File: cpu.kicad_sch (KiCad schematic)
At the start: 50 parts, among them IC12 DS2401+, IC13 ARM250, IC20 74HC138, IC27 74AC32, IC8 74HCT14, X100 40.0MHz, X4 72.0MHz, X5 25.175MHz

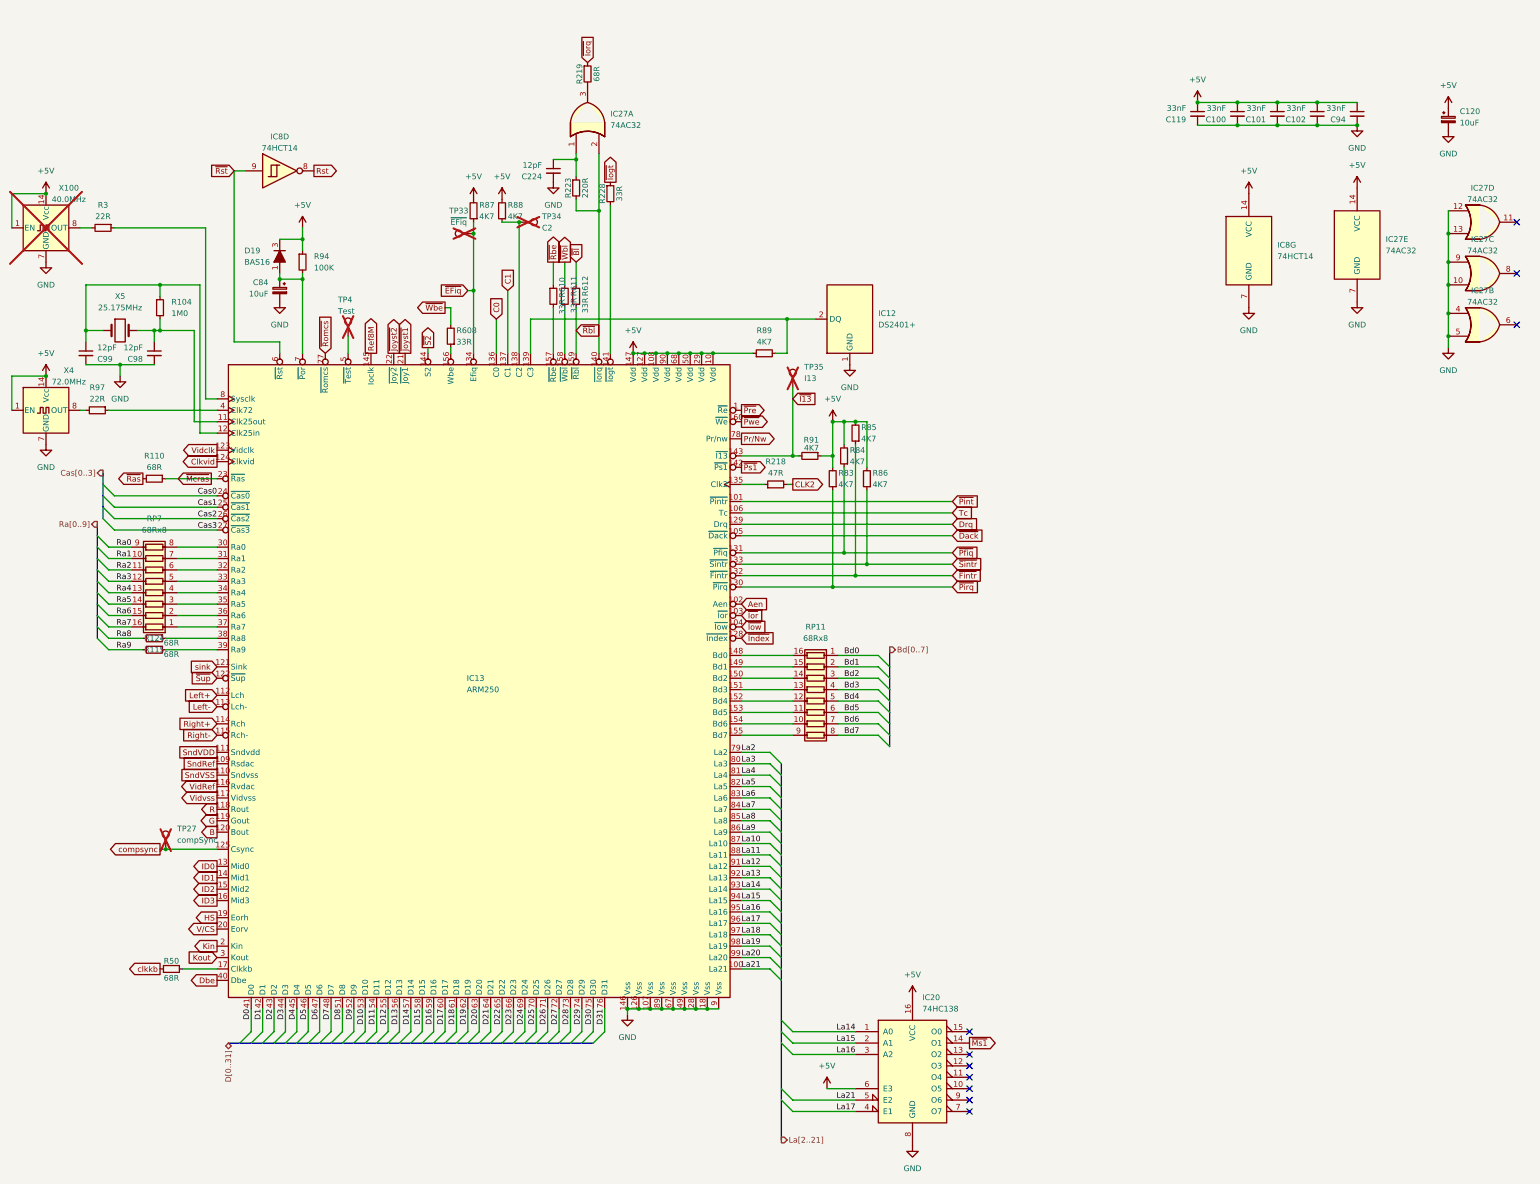
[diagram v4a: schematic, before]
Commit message: verify all component values vs TRM
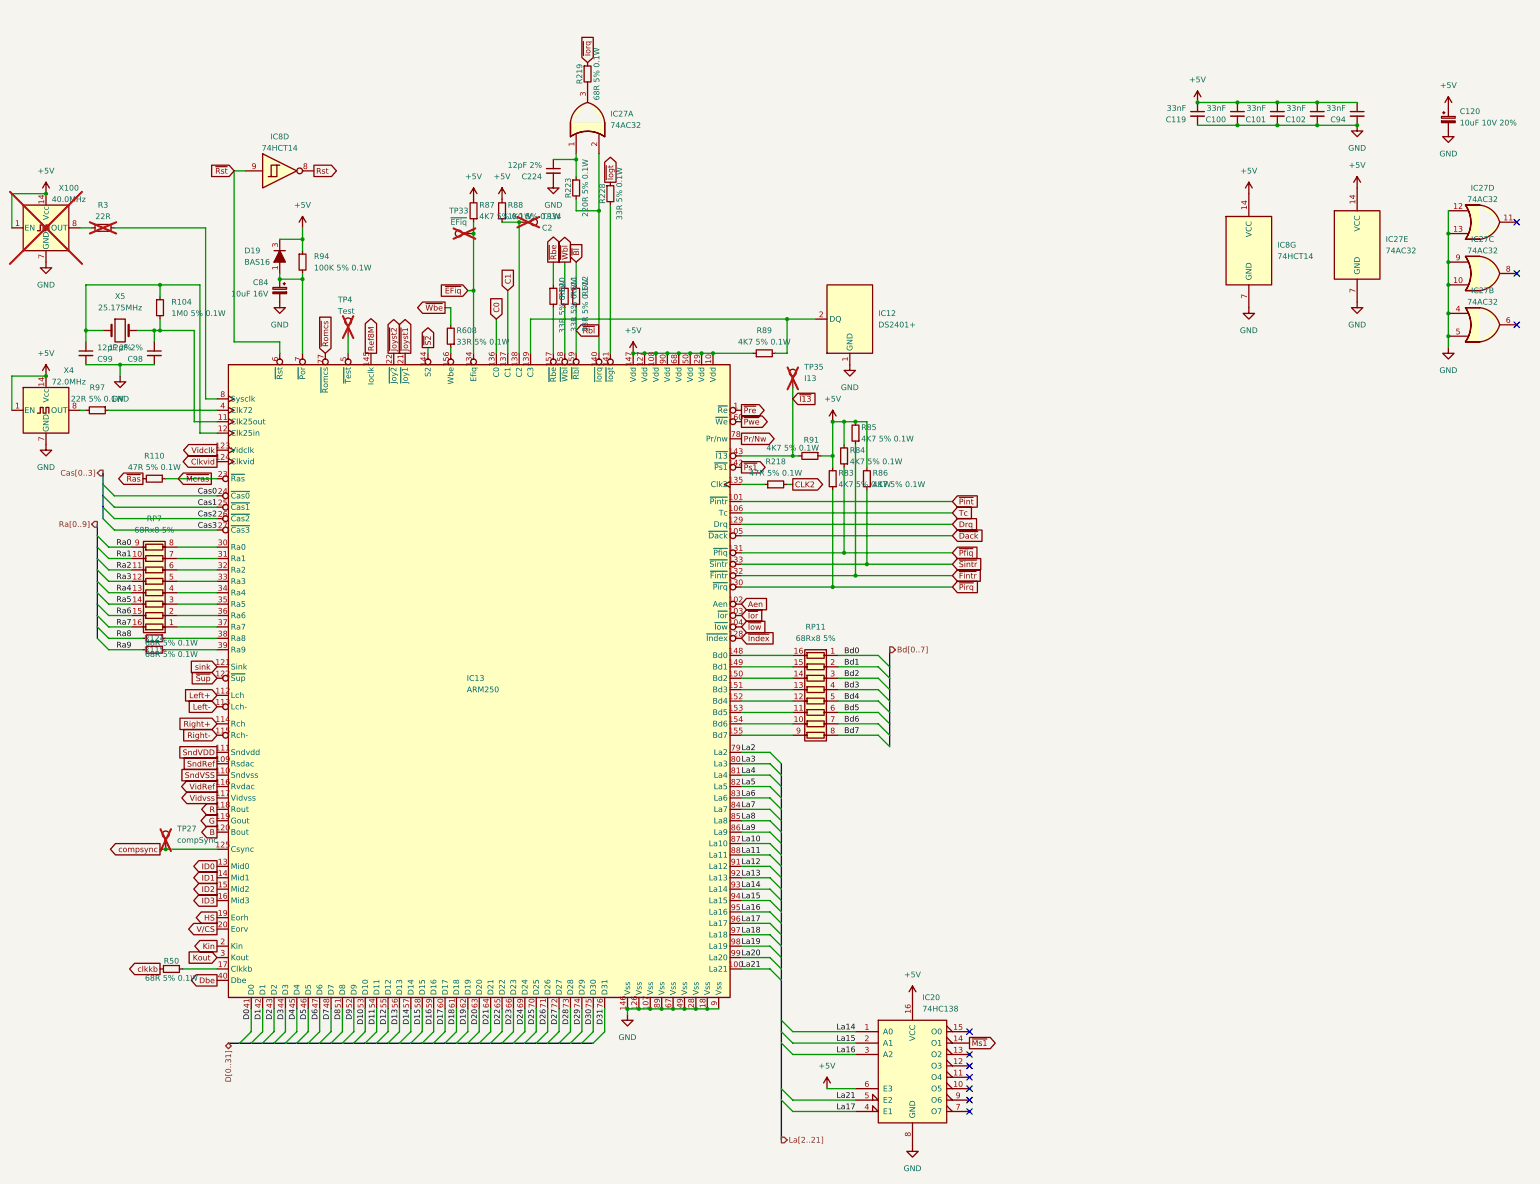
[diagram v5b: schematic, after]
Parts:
- C120: value 10uF -> 10uF 10V 20%
- C224, C98, C99: value 12pF -> 12pF 2%
- C84: value 10uF -> 10uF 16V
- R104: value 1M0 -> 1M0 5% 0.1W
- R110: value 68R -> 47R 5% 0.1W
- R115, R124, R219, R50: value 68R -> 68R 5% 0.1W
- R218: value 47R -> 47R 5% 0.1W
- R223: value 220R -> 220R 5% 0.1W
- R228, R608, R610, R611, R612: value 33R -> 33R 5% 0.1W
- R3: now not fitted; now left out of the parts list
- R83, R84, R85, R86, R87, R89, R91: value 4K7 -> 4K7 5% 0.1W
- R88: value 4K7 -> 1K0 5% 0.1W
- R94: value 100K -> 100K 5% 0.1W
- R97: value 22R -> 22R 5% 0.1W
- RP11, RP7: value 68Rx8 -> 68Rx8 5%
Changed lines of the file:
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@@
 			)
 		)
-		(property "Value" "68R"
+		(property "Value" "68R 5% 0.1W"
 			(at 177.292 24.13 90)
 			(effects
@@
 			)
 		)
-		(property "Value" "68R"
+		(property "Value" "68R 5% 0.1W"
 			(at 82.55 225.552 90)
 			(effects
@@
 			)
 		)
-		(property "Value" "68Rx8"
+		(property "Value" "68Rx8 5%"
 			(at 226.06 149.86 90)
 			(effects
@@
 			)
 		)
-		(property "Value" "10uF"
+		(property "Value" "10uF 10V 20%"
 			(at 369.57 35.0138 0)
 			(effects
@@
 			)
 		)
-		(property "Value" "1M0"
+		(property "Value" "1M0 5% 0.1W"
 			(at 82.55 77.4699 0)
 			(effects
@@
 			)
 		)
-		(property "Value" "4K7"
+		(property "Value" "4K7 5% 0.1W"
 			(at 214.63 83.82 90)
 			(effects
@@
 			)
 		)
-		(property "Value" "33R"
+		(property "Value" "33R 5% 0.1W"
 			(at 169.6123 75.9878 90)
 			(effects
@@
 			)
 		)
-		(property "Value" "68R"
+		(property "Value" "68R 5% 0.1W"
 			(at 82.55 150.876 90)
 			(effects
@@
 		(unit 1)
 		(exclude_from_sim no)
-		(in_bom yes)
+		(in_bom no)
 		(on_board yes)
-		(dnp no)
+		(dnp yes)
 		(fields_autoplaced yes)
 		(property "Reference" "R3"
@@
 			)
 		)
-		(property "Value" "33R"
+		(property "Value" "33R 5% 0.1W"
 			(at 182.372 50.8 90)
 			(effects
@@
 			)
 		)
-		(property "Value" "47R"
+		(property "Value" "47R 5% 0.1W"
 			(at 217.17 113.03 90)
 			(effects
@@
 			)
 		)
-		(property "Value" "68R"
+		(property "Value" "68R 5% 0.1W"
 			(at 82.55 153.416 90)
 			(effects
@@
 			)
 		)
-		(property "Value" "100K"
+		(property "Value" "100K 5% 0.1W"
 			(at 114.3 67.3099 0)
 			(effects
@@
 			)
 		)
-		(property "Value" "12pF"
+		(property "Value" "12pF 2%"
 			(at 165.1 44.4565 0)
 			(effects
@@
 			)
 		)
-		(property "Value" "220R"
+		(property "Value" "220R 5% 0.1W"
 			(at 174.752 49.53 90)
 			(effects
@@
 			)
 		)
-		(property "Value" "33R"
+		(property "Value" "33R 5% 0.1W"
 			(at 146.05 83.82 0)
 			(effects
@@
 			)
 		)
-		(property "Value" "4K7"
+		(property "Value" "1K0 5% 0.1W"
 			(at 157.48 55.88 0)
 			(effects
@@
 			)
 		)
-		(property "Value" "4K7"
+		(property "Value" "4K7 5% 0.1W"
 			(at 151.13 55.88 0)
 			(effects
@@
 			)
 		)
-		(property "Value" "4K7"
+		(property "Value" "4K7 5% 0.1W"
 			(at 231.14 115.57 0)
 			(effects
@@
 			)
 		)
-		(property "Value" "12pF"
+		(property "Value" "12pF 2%"
 			(at 76.2 85.0965 0)
 			(effects
@@
 			)
 		)
-		(property "Value" "68R"
+		(property "Value" "47R 5% 0.1W"
 			(at 78.74 111.76 90)
 			(effects
@@
 			)
 		)
-		(property "Value" "4K7"
+		(property "Value" "4K7 5% 0.1W"
 			(at 238.76 115.57 0)
 			(effects
@@
 			)
 		)
-		(property "Value" "33R"
+		(property "Value" "33R 5% 0.1W"
 			(at 174.752 75.692 90)
 			(effects
@@
 			)
 		)
-		(property "Value" "4K7"
+		(property "Value" "4K7 5% 0.1W"
 			(at 233.68 110.49 0)
 			(effects
@@
 			)
 		)
-		(property "Value" "68Rx8"
+		(property "Value" "68Rx8 5%"
 			(at 78.74 125.73 90)
 			(effects
@@
 			)
 		)
-		(property "Value" "4K7"
+		(property "Value" "4K7 5% 0.1W"
 			(at 226.822 107.442 90)
 			(effects
@@
 			)
 		)
-		(property "Value" "33R"
+		(property "Value" "33R 5% 0.1W"
 			(at 172.212 75.692 90)
 			(effects
@@
 			)
 		)
-		(property "Value" "22R"
+		(property "Value" "22R 5% 0.1W"
 			(at 66.04 96.52 90)
 			(effects
@@
 			)
 		)
-		(property "Value" "10uF"
+		(property "Value" "10uF 16V"
 			(at 104.14 73.1138 0)
 			(effects
@@
 			)
 		)
-		(property "Value" "4K7"
+		(property "Value" "4K7 5% 0.1W"
 			(at 236.22 105.41 0)
 			(effects
@@
 			)
 		)
-		(property "Value" "12pF"
+		(property "Value" "12pF 2%"
 			(at 66.04 85.0965 0)
 			(effects

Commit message: fix qfp footprints, restore CAS filters
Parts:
- IC13: footprint Package_QFP:PQFP-160_28x28mm_P0.65mm -> Acorn:PQFP-160_28x28mm_P0.65mm
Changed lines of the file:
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@@
 			)
 		)
-		(property "Footprint" "Package_QFP:PQFP-160_28x28mm_P0.65mm"
+		(property "Footprint" "Acorn:PQFP-160_28x28mm_P0.65mm"
 			(at 151.384 161.798 0)
 			(effects

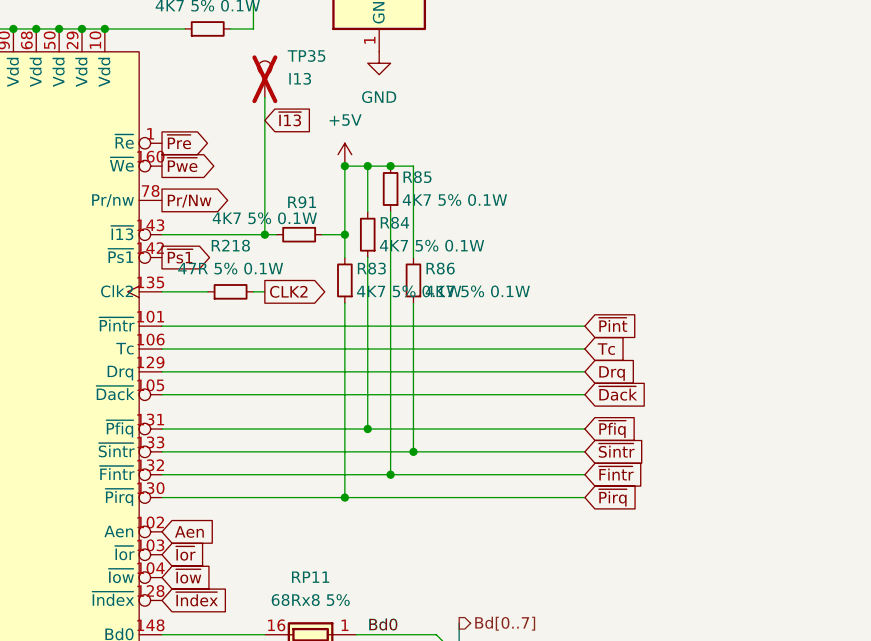
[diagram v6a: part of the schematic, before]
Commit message: fix VGA port footprint
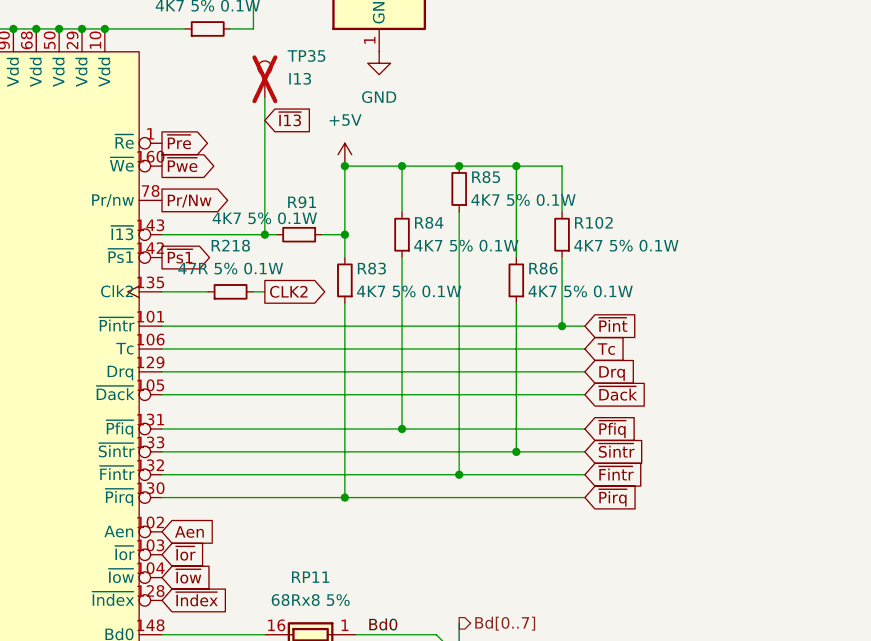
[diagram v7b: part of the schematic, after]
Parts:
- added R102: 4K7 5% 0.1W, Resistor_SMD:R_0805_2012Metric, symbol Device:R_Small
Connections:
- net +5V: now also R102.2
- net ~{Pint}: now also R102.1
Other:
- moved on the sheet: R84, R85, R86
